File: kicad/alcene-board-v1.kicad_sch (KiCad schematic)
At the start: 8 parts, among them J1 ESP32-S3-DevKitC-1_J1, J2 USB-C Input, J3 ESP32-S3-DevKitC-1_J3, J4 ILI9341_TFT_14pin

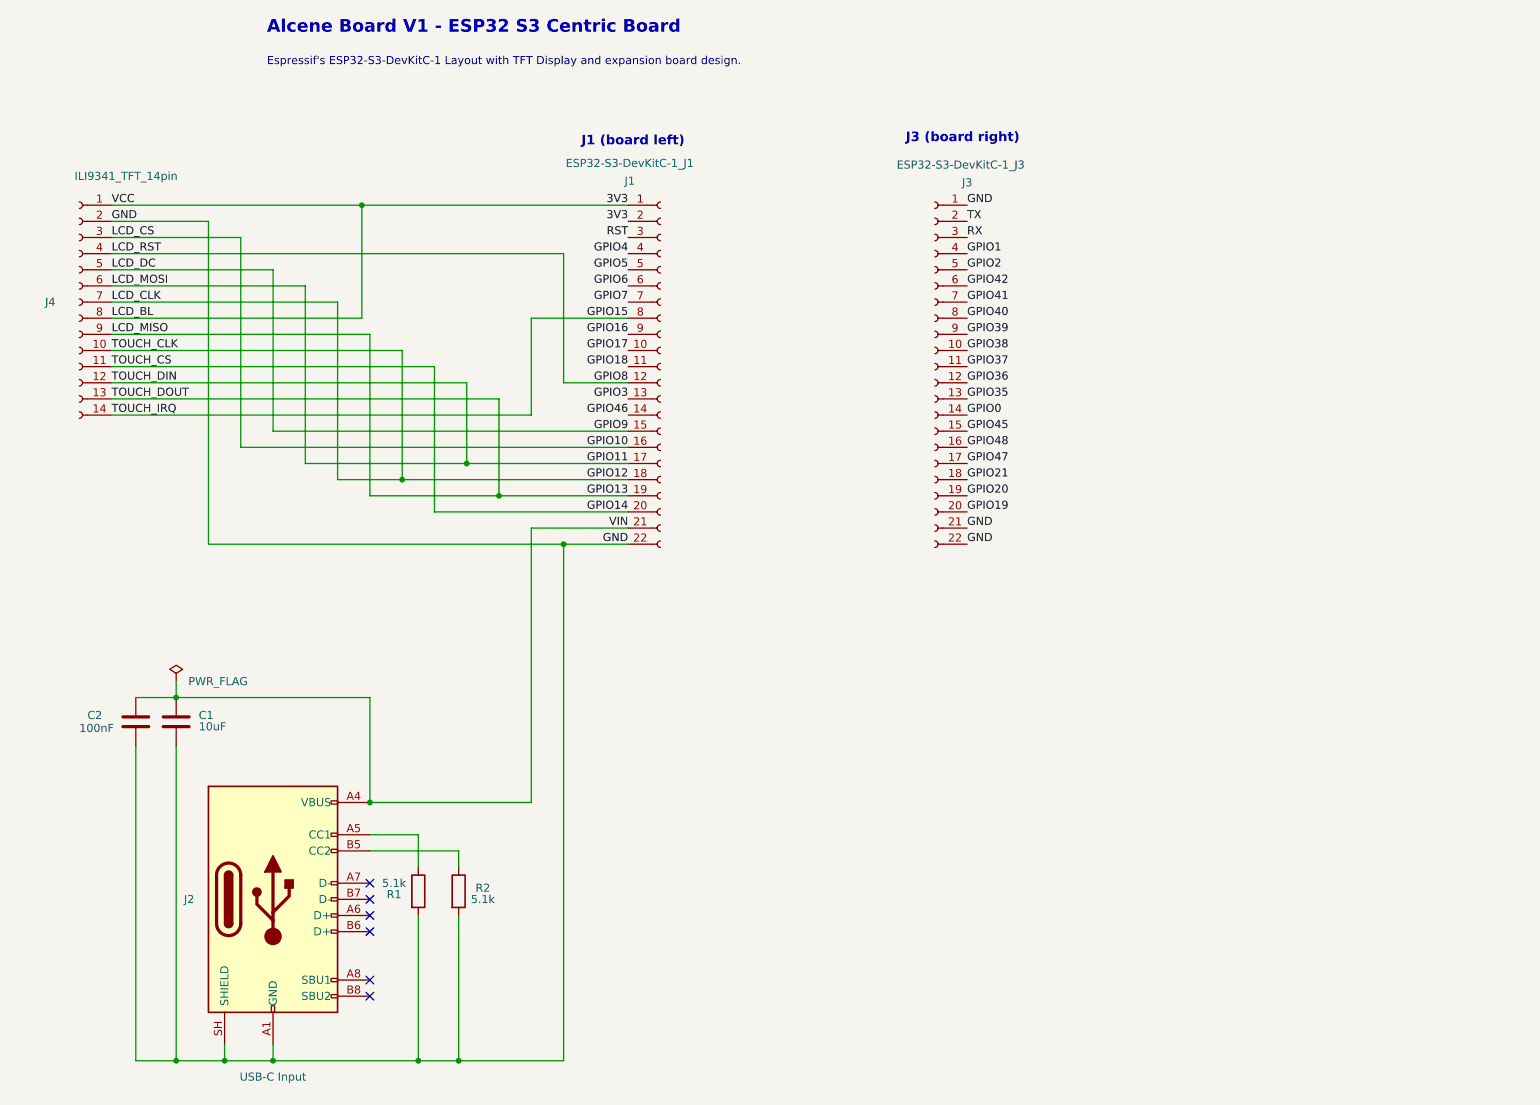
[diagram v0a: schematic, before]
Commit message: feat: pin breakout and momentary RST
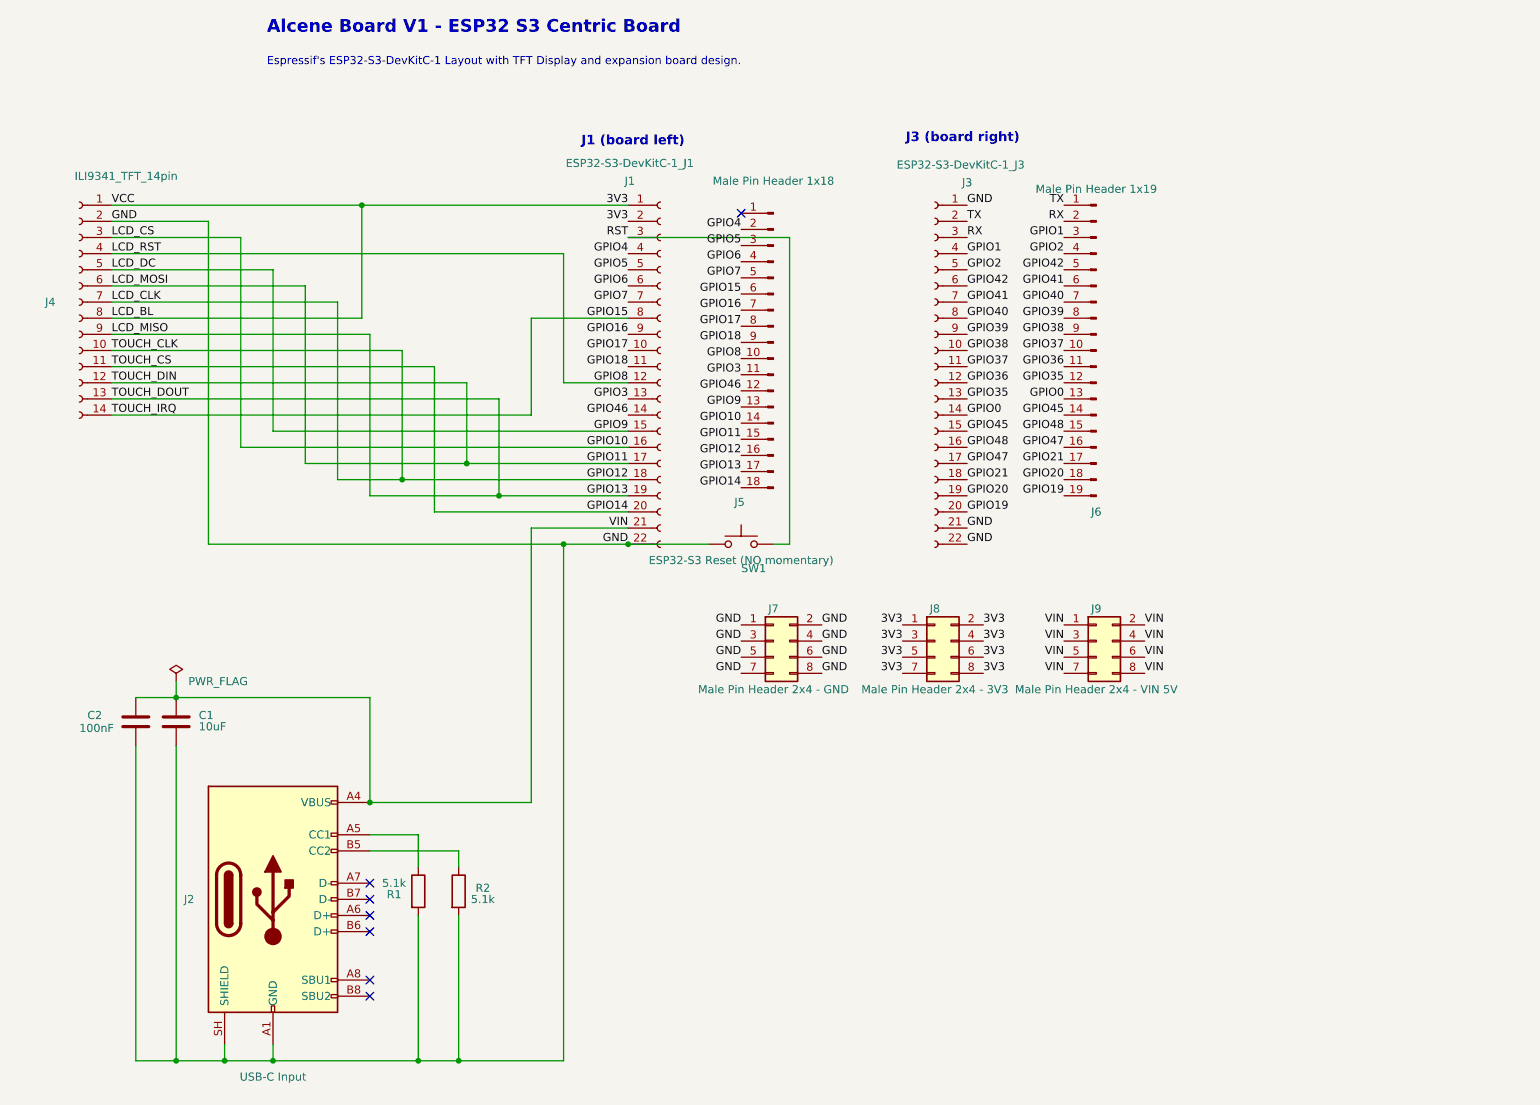
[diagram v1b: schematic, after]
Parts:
- added J5: Male Pin Header 1x18, Connector_PinHeader_2.54mm:PinHeader_1x18_P2.54mm_Vertical, symbol Connector:Conn_01x18_Pin
- added J6: Male Pin Header 1x19, Connector_PinHeader_2.54mm:PinHeader_1x19_P2.54mm_Vertical, symbol Connector:Conn_01x19_Pin
- added J7: Male Pin Header 2x4 - GND, Connector_PinHeader_2.54mm:PinHeader_2x04_P2.54mm_Vertical, symbol Connector_Generic:Conn_02x04_Odd_Even
- added J8: Male Pin Header 2x4 - 3V3, Connector_PinHeader_2.54mm:PinHeader_2x04_P2.54mm_Vertical, symbol Connector_Generic:Conn_02x04_Odd_Even
- added J9: Male Pin Header 2x4 - VIN 5V, Connector_PinHeader_2.54mm:PinHeader_2x04_P2.54mm_Vertical, symbol Connector_Generic:Conn_02x04_Odd_Even
- added SW1: ESP32-S3 Reset (NO momentary), Button_Switch_SMD:SW_Push_SPST_NO_Alps_SKRK, symbol Switch:SW_Push
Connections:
- net 3V3: now also J8.1 (Pin_1), J8.2 (Pin_2), J8.3 (Pin_3), J8.4 (Pin_4), J8.5 (Pin_5), J8.6 (Pin_6), J8.7 (Pin_7), J8.8 (Pin_8)
- net GND: now also J7.1 (Pin_1), J7.2 (Pin_2), J7.3 (Pin_3), J7.4 (Pin_4), J7.5 (Pin_5), J7.6 (Pin_6), J7.7 (Pin_7), J7.8 (Pin_8), SW1.1
- net GPIO0: now also J6.13 (Pin_13)
- net GPIO1: now also J6.3 (Pin_3)
- net GPIO10: now also J5.14 (Pin_14)
- net GPIO11: now also J5.15 (Pin_15)
- net GPIO12: now also J5.16 (Pin_16)
- net GPIO13: now also J5.17 (Pin_17)
- net GPIO14: now also J5.18 (Pin_18)
- net GPIO15: now also J5.6 (Pin_6)
- net GPIO16: now also J5.7 (Pin_7)
- net GPIO17: now also J5.8 (Pin_8)
- net GPIO18: now also J5.9 (Pin_9)
- net GPIO19: now also J6.19 (Pin_19)
- net GPIO2: now also J6.4 (Pin_4)
- net GPIO20: now also J6.18 (Pin_18)
- net GPIO21: now also J6.17 (Pin_17)
- net GPIO3: now also J5.11 (Pin_11)
- net GPIO35: now also J6.12 (Pin_12)
- net GPIO36: now also J6.11 (Pin_11)
- net GPIO37: now also J6.10 (Pin_10)
- net GPIO38: now also J6.9 (Pin_9)
- net GPIO39: now also J6.8 (Pin_8)
- net GPIO4: now also J5.2 (Pin_2)
- net GPIO40: now also J6.7 (Pin_7)
- net GPIO41: now also J6.6 (Pin_6)
- net GPIO42: now also J6.5 (Pin_5)
- net GPIO45: now also J6.14 (Pin_14)
- net GPIO46: now also J5.12 (Pin_12)
- net GPIO47: now also J6.16 (Pin_16)
- net GPIO48: now also J6.15 (Pin_15)
- net GPIO5: now also J5.3 (Pin_3)
- net GPIO6: now also J5.4 (Pin_4)
- net GPIO7: now also J5.5 (Pin_5)
- net GPIO8: now also J5.10 (Pin_10)
- net GPIO9: now also J5.13 (Pin_13)
- net RST: now also SW1.2
- net RX: now also J6.2 (Pin_2)
- net TX: now also J6.1 (Pin_1)
- net VIN: now also J9.1 (Pin_1), J9.2 (Pin_2), J9.3 (Pin_3), J9.4 (Pin_4), J9.5 (Pin_5), J9.6 (Pin_6), J9.7 (Pin_7), J9.8 (Pin_8)
- no-connect marks 6 -> 7

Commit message: feat: broke out headers
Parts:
- removed J6: Male Pin Header 1x19, Connector_PinHeader_2.54mm:PinHeader_1x19_P2.54mm_Vertical, symbol Connector:Conn_01x19_Pin
- added J6: Male Pin Header 1x18 - J3 Signals, Connector_PinHeader_2.54mm:PinHeader_1x18_P2.54mm_Vertical, symbol Connector:Conn_01x18_Pin
- J5: value Male Pin Header 1x18 -> Male Pin Header 1x18 - J1 Signals
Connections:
- net GPIO0: now also J6.13 (Pin_13)
- net GPIO1: now also J6.3 (Pin_3)
- net GPIO19: now also J5.1 (Pin_1)
- net GPIO2: now also J6.4 (Pin_4)
- net GPIO20: now also J6.18 (Pin_18)
- net GPIO21: now also J6.17 (Pin_17)
- net GPIO35: now also J6.12 (Pin_12)
- net GPIO36: now also J6.11 (Pin_11)
- net GPIO37: now also J6.10 (Pin_10)
- net GPIO38: now also J6.9 (Pin_9)
- net GPIO39: now also J6.8 (Pin_8)
- net GPIO40: now also J6.7 (Pin_7)
- net GPIO41: now also J6.6 (Pin_6)
- net GPIO42: now also J6.5 (Pin_5)
- net GPIO45: now also J6.14 (Pin_14)
- net GPIO47: now also J6.16 (Pin_16)
- net GPIO48: now also J6.15 (Pin_15)
- net RX: now also J6.2 (Pin_2)
- net TX: now also J6.1 (Pin_1)
- no-connect marks 7 -> 6

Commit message: feat: PCB approved schematic
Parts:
- C1: Dielectric (none) -> X7R; MPN (none) -> GRM21BZ71E106KE15L; Manufacturer (none) -> Murata Electronics; Package (none) -> 0805 (2012 metric); Tolerance (none) -> +/-10%; Voltage (none) -> 25 V
- C2: Dielectric (none) -> X7R; MPN (none) -> GRM21BR71H104KA01L; Manufacturer (none) -> Murata Electronics; Package (none) -> 0805 (2012 metric); Tolerance (none) -> +/-10%; Voltage (none) -> 50 V
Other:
- note added: "J4 ILI9341 TFT pin functions: 1 3V3 (VCC) 2 GND 3 GPIO10 (LCD_CS) 4 GPIO8 (LCD_RST) 5 GPIO9 (LCD_DC) 6 GPIO11 (LCD_MOSI) 7 GPIO12 (LCD_CLK) 8 3V3 (LCD_BL, owner-confirmed direct) 9 GPIO13 (LCD_MISO) 10 GPIO12 (TOUCH_CLK) 11 GPIO14 (TOUCH_CS) 12 GPIO11 (TOUCH_DIN) 13 GPIO13 (TOUCH_DOUT) 14 GPIO15 (TOUCH_IRQ)"
- note added: "Power architecture notes: J2 USB-C is the external power input. J8 3V3 and J9 VIN are distribution outputs only. Do not inject external power through these headers. Do not connect J2 USB power and DevKit native USB power simultaneously. DevKit power inputs are mutually exclusive. Direct VBUS-to-VIN connection; reverse-current blocking is not provided."
- note added: "USB-C VBUS INPUT"
